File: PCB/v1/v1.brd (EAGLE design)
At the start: 53 x 39 mm, 62 parts, among them U2 AT24C512C-SHD-B

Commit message: just needs an RF antenna
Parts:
- moved WAKE 10.6 mm to (41.6, 27.1)
- moved C5 3.82 mm to (41.2, 21.8)
- moved U$4 2.50 mm to (43.3, 23.1)
- moved C9 1.82 mm to (37.8, 21.5)
- moved L2 1.27 mm to (39.4, 20.8)
- moved U$3 0.75 mm to (32.3, 31.5)
- moved C17 0.62 mm to (41.2, 19.8), turned to 180 degrees
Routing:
- net GND: track 118.8 -> 184.4 mm, vias 4 -> 9
- net N$39: track 37.8 -> 48.5 mm, vias 2 -> 0
- net N$49: track 23.7 -> 13.5 mm
- net N$21: track 143.0 -> 135.9 mm
- net N$34: track 93.1 -> 97.2 mm
- net N$32: track 7.46 -> 11.2 mm
- net N$22: track 123.2 -> 126.4 mm
- net N$27: track 11.9 -> 14.5 mm
- net N$28: track 32.5 -> 34.8 mm
- net N$36: track 7.32 -> 9.27 mm, vias 0 -> 1
- net N$45: track 11.1 -> 12.8 mm, vias 0 -> 1
- net N$26: track 15.1 -> 16.8 mm

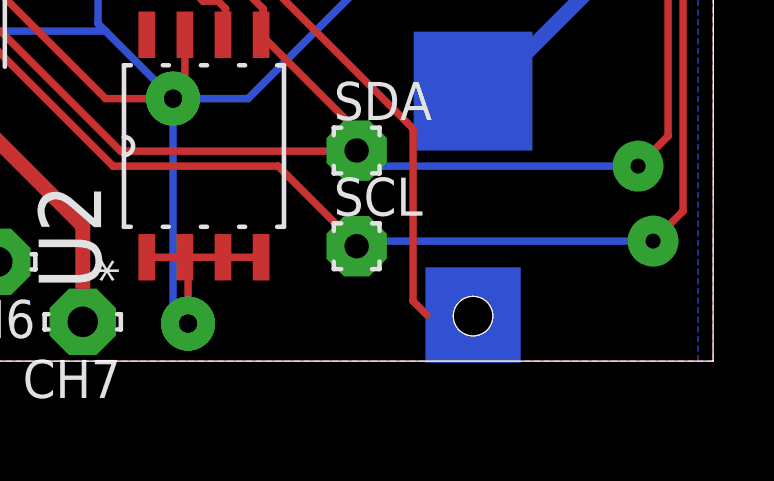
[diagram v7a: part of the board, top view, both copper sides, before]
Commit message: just needs an RF F-antenna
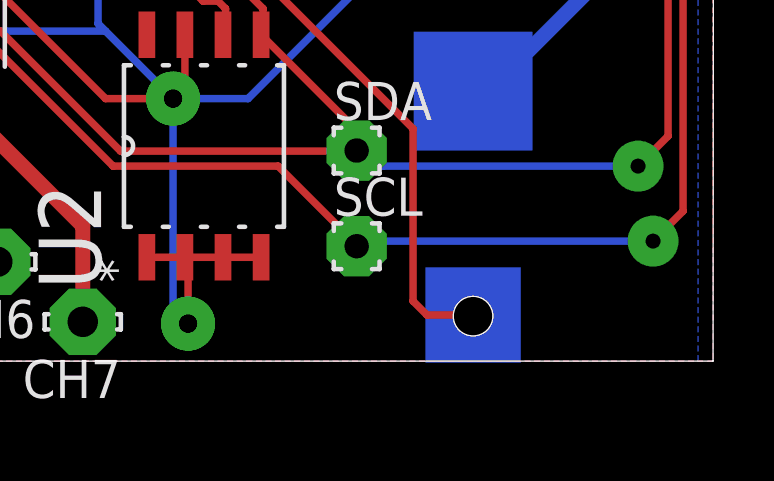
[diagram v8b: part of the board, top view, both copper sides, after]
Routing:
- net N$34: track 97.2 -> 98.7 mm
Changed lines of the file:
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@@
 <wire x1="40" y1="25.25" x2="45.25" y2="25.25" width="0.25" layer="1"/>
 <wire x1="45.25" y1="25.25" x2="45.5" y2="25" width="0.25" layer="1"/>
-<wire x1="45.25" y1="25.25" x2="45" y2="29.5" width="0" layer="19" extent="1-16"/>
-<wire x1="1.25" y1="1.5" x2="1.129740625" y2="2.612" width="0" layer="19" extent="1-1"/>
-<wire x1="36.665" y1="3.4616" x2="35.5" y2="3.3566" width="0" layer="19" extent="1-1"/>
-<wire x1="7.004740625" y1="2.612" x2="6" y2="4.25" width="0" layer="19" extent="1-1"/>
-<wire x1="31.76155" y1="26.062" x2="31.56" y2="19.7374" width="0" layer="19" extent="1-1"/>
+<wire x1="6" y1="4.25" x2="7.004740625" y2="2.612" width="0" layer="19" extent="1-1"/>
 </signal>
 <signal name="N$28">
@@
 <wire x1="40.6774" y1="19.75" x2="40.6774" y2="20.04425" width="0.25" layer="1"/>
 <wire x1="40.6774" y1="20.04425" x2="39.87405" y2="20.8476" width="0.25" layer="1"/>
-<wire x1="43.4625" y1="1.5375" x2="45" y2="1.5375" width="0" layer="19" extent="1-16"/>
+<wire x1="43.4625" y1="1.5375" x2="45" y2="1.5375" width="0.25" layer="1"/>
+<wire x1="45" y1="1.5375" x2="45" y2="1.5375" width="0" layer="19" extent="1-16"/>
 </signal>
 <signal name="N$31">
